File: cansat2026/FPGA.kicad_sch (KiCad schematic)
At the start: 16 parts, among them U1001 ICE5LP1K-SG48

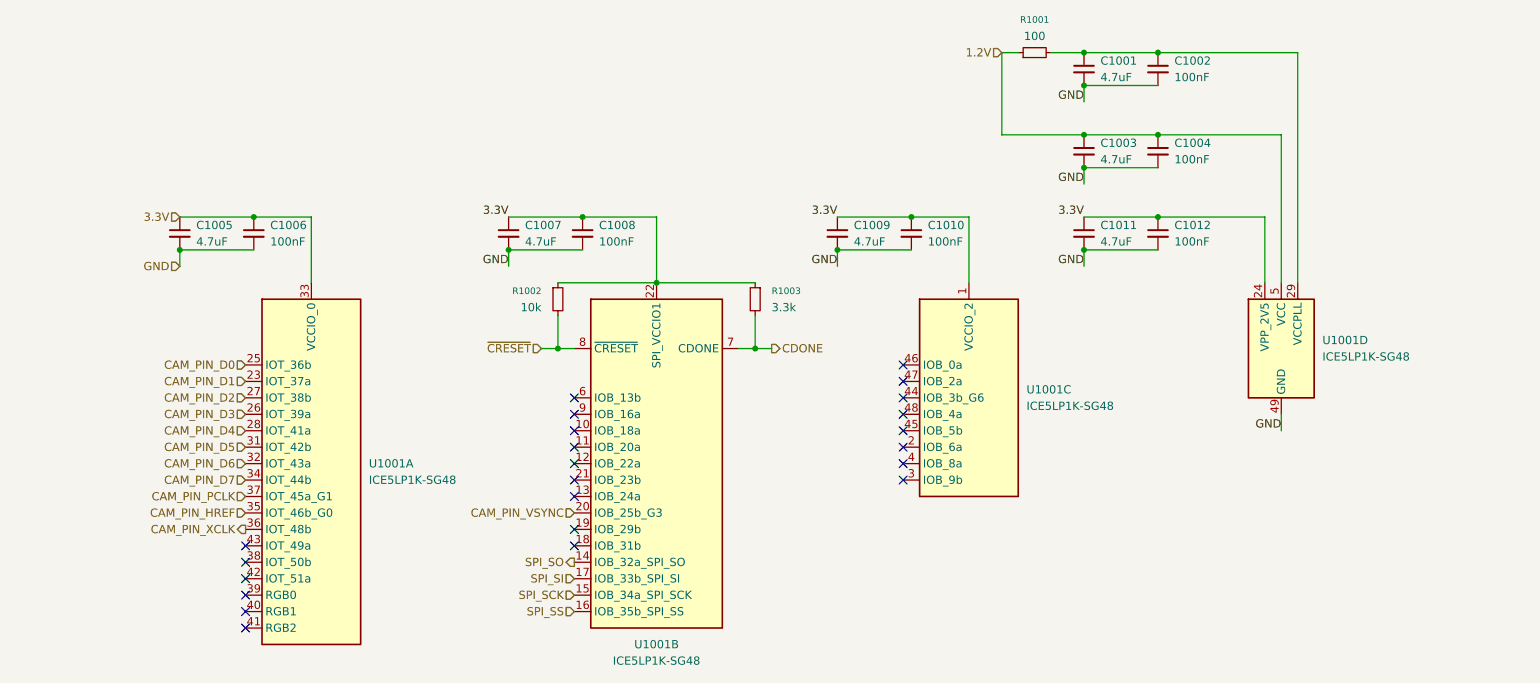
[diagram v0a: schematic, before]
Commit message: Update: いろいろした
GPS変えた
USB追加した
気圧センサ変えた
FPGA変えた
MDにキャパシタ追加した
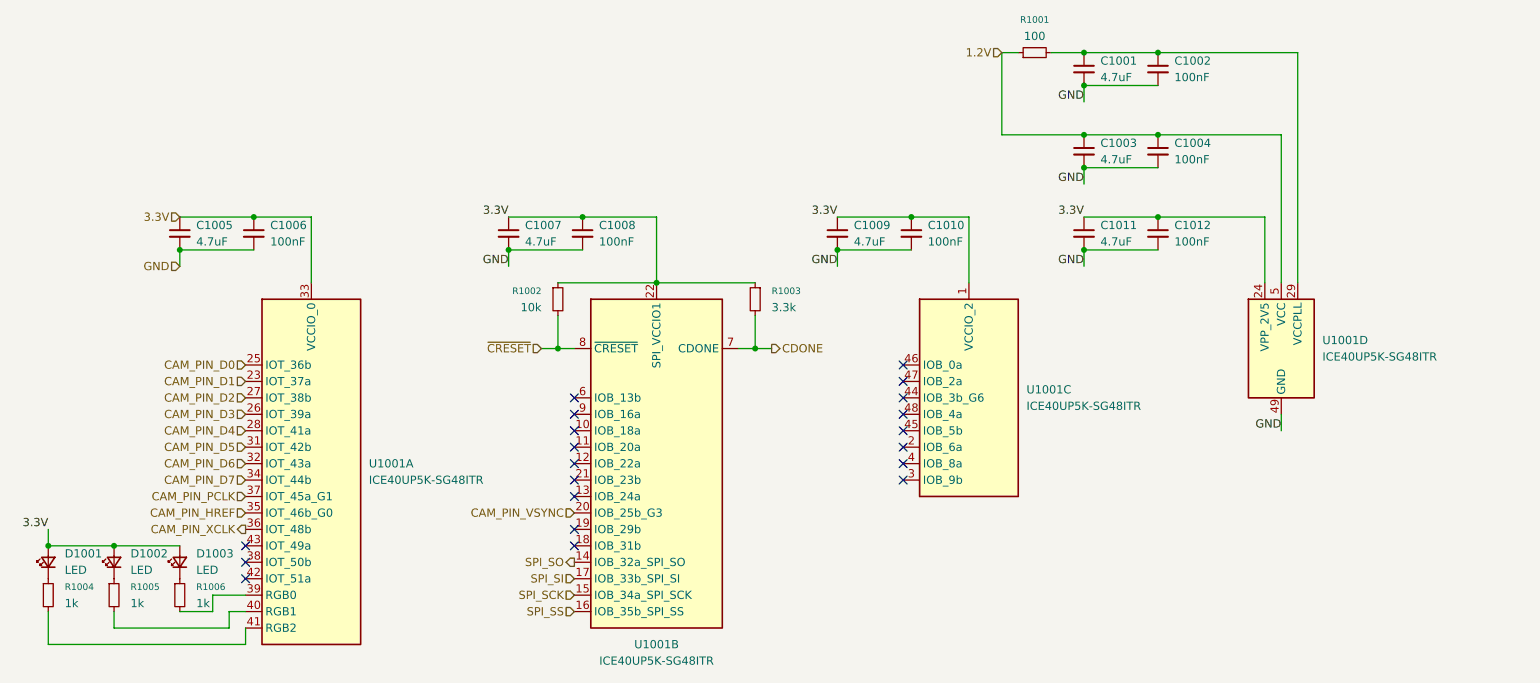
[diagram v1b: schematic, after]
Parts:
- removed U1001: ICE5LP1K-SG48, Package_DFN_QFN:QFN-48-1EP_7x7mm_P0.5mm_EP5.6x5.6mm, symbol FPGA_Lattice:ICE5LP1K-SG48
- added D1001, D1002, D1003: LED, LED_SMD:LED_0603_1608Metric, symbol Device:LED_Small
- added R1004, R1005, R1006: 1k, Resistor_SMD:R_0402_1005Metric, symbol Device:R_Small
- added U1001: ICE40UP5K-SG48ITR, Package_DFN_QFN:QFN-48-1EP_7x7mm_P0.5mm_EP5.6x5.6mm, symbol FPGA_Lattice:ICE40UP5K-SG48ITR
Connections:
- net 1.2V: now also U1001.30 (VCC), U1001.5 (VCC)
- net 3.3V: now also D1001.2 (A), D1002.2 (A), D1003.2 (A), U1001.1 (VCCIO_2), U1001.22 (SPI_VCCIO1), U1001.24 (VPP_2V5), U1001.33 (VCCIO_0)
- net CAM_PIN_D0: now also U1001.25 (IOT_36b)
- net CAM_PIN_D1: now also U1001.23 (IOT_37a)
- net CAM_PIN_D2: now also U1001.27 (IOT_38b)
- net CAM_PIN_D3: now also U1001.26 (IOT_39a)
- net CAM_PIN_D4: now also U1001.28 (IOT_41a)
- net CAM_PIN_D5: now also U1001.31 (IOT_42b)
- net CAM_PIN_D6: now also U1001.32 (IOT_43a)
- net CAM_PIN_D7: now also U1001.34 (IOT_44b)
- net CAM_PIN_HREF: now also U1001.35 (IOT_46b_G0)
- net CAM_PIN_PCLK: now also U1001.37 (IOT_45a_G1)
- net CAM_PIN_VSYNC: now also U1001.20 (IOB_25b_G3)
- net CAM_PIN_XCLK: now also U1001.36 (IOT_48b)
- net CDONE: now also U1001.7 (CDONE)
- net GND: now also U1001.49 (GND)
- net SPI_SCK: now also U1001.15 (IOB_34a_SPI_SCK)
- net SPI_SI: now also U1001.17 (IOB_33b_SPI_SI)
- net SPI_SO: now also U1001.14 (IOB_32a_SPI_SO)
- net SPI_SS: now also U1001.16 (IOB_35b_SPI_SS)
- net ~{CRESET}: now also U1001.8 (~{CRESET})
- net at C1001.1, C1002.1, R1001.2: now also U1001.29 (VCCPLL)
- new net: D1001.1 (K), R1004.1
- new net: R1004.2, U1001.41 (RGB2)
- new net: D1003.1 (K), R1006.1
- new net: R1006.2, U1001.39 (RGB0)
- new net: D1002.1 (K), R1005.1
- new net: R1005.2, U1001.40 (RGB1)
- no-connect marks 23 -> 20

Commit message: Update: 完成した
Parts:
- added C1005: 4.7uF, Capacitor_SMD:C_0402_1005Metric, symbol Device:C_Small
- added C1006: 100nF, Capacitor_SMD:C_0402_1005Metric, symbol Device:C_Small
- added JP1001: I2C Addr, Jumper:SolderJumper-3_P1.3mm_Bridged12_RoundedPad1.0x1.5mm_NumberLabels, symbol Jumper:SolderJumper_3_Bridged12
- renumbered C1005 to C1007, C1006 to C1008, C1007 to C1009, C1008 to C1010, C1009 to C1011, C1010 to C1012, C1011 to C1013, C1012 to C1014
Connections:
- net 1.2V: now also C1005.1, C1006.1
- net 3.3V: now also JP1001.3 (B); no longer C1007.1, C1008.1, U1001.33 (VCCIO_0)
- net CAM_PIN_D0: now also U1001.23 (IOT_37a); no longer U1001.25 (IOT_36b)
- net CAM_PIN_D1: now also U1001.25 (IOT_36b); no longer U1001.23 (IOT_37a)
- net CAM_PIN_D2: now also U1001.26 (IOT_39a); no longer U1001.27 (IOT_38b)
- net CAM_PIN_D3: now also U1001.27 (IOT_38b); no longer U1001.26 (IOT_39a)
- net CAM_PIN_HREF: now also U1001.37 (IOT_45a_G1); no longer U1001.35 (IOT_46b_G0)
- net CAM_PIN_PCLK: now also U1001.35 (IOT_46b_G0); no longer U1001.37 (IOT_45a_G1)
- net CAM_PIN_VSYNC: now also U1001.38 (IOT_50b); no longer U1001.20 (IOB_25b_G3)
- net GND: now also C1005.2, C1006.2
- net CP_CAM_PIN_VSYNC: now reaches U1001.2 (IOB_6a)
- net CP_CAM_PIN_RESET: now reaches U1001.3 (IOB_9b)
- net CP_CAM_PIN_PWDN: now reaches U1001.4 (IOB_8a)
- net LS_EN: now reaches U1001.46 (IOB_0a)
- net CP_CAM_PIN_D2: now reaches U1001.10 (IOB_18a)
- net CP_CAM_PIN_D3: now reaches U1001.11 (IOB_20a)
- net CP_CAM_PIN_D4: now reaches U1001.12 (IOB_22a)
- net CP_CAM_PIN_D6: now reaches U1001.13 (IOB_24a)
- net CP_CAM_PIN_D7: now reaches U1001.18 (IOB_31b)
- net CP_CAM_PIN_HREF: now reaches U1001.19 (IOB_29b)
- net CP_CAM_PIN_D5: now reaches U1001.21 (IOB_23b)
- net CP_CAM_PIN_D0: now reaches U1001.6 (IOB_13b)
- net CP_CAM_PIN_D1: now reaches U1001.9 (IOB_16a)
- new net: C1007.1, C1008.1, JP1001.2 (C), U1001.33 (VCCIO_0)
- new net 1.8V: JP1001.1 (A)
- new net CP_CAM_PIN_PCLK: U1001.20 (IOB_25b_G3)
- no-connect marks 20 -> 6
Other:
- moved on the sheet: C1001, C1002, C1003, C1004, C1009, C1010, C1011, C1012, C1013, C1014, D1001, D1002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
